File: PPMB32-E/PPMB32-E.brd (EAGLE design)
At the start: 78.7 x 82.2 mm, 11 parts, among them IC1 7805TV, IC2 LM3940IT-3.3, K1 ARK500/2, K2 ARK500/2, K3 ARK500/2, K4 ARK500/2, K5 ARK500/2, U1 ESP32-DEVKITC-32D

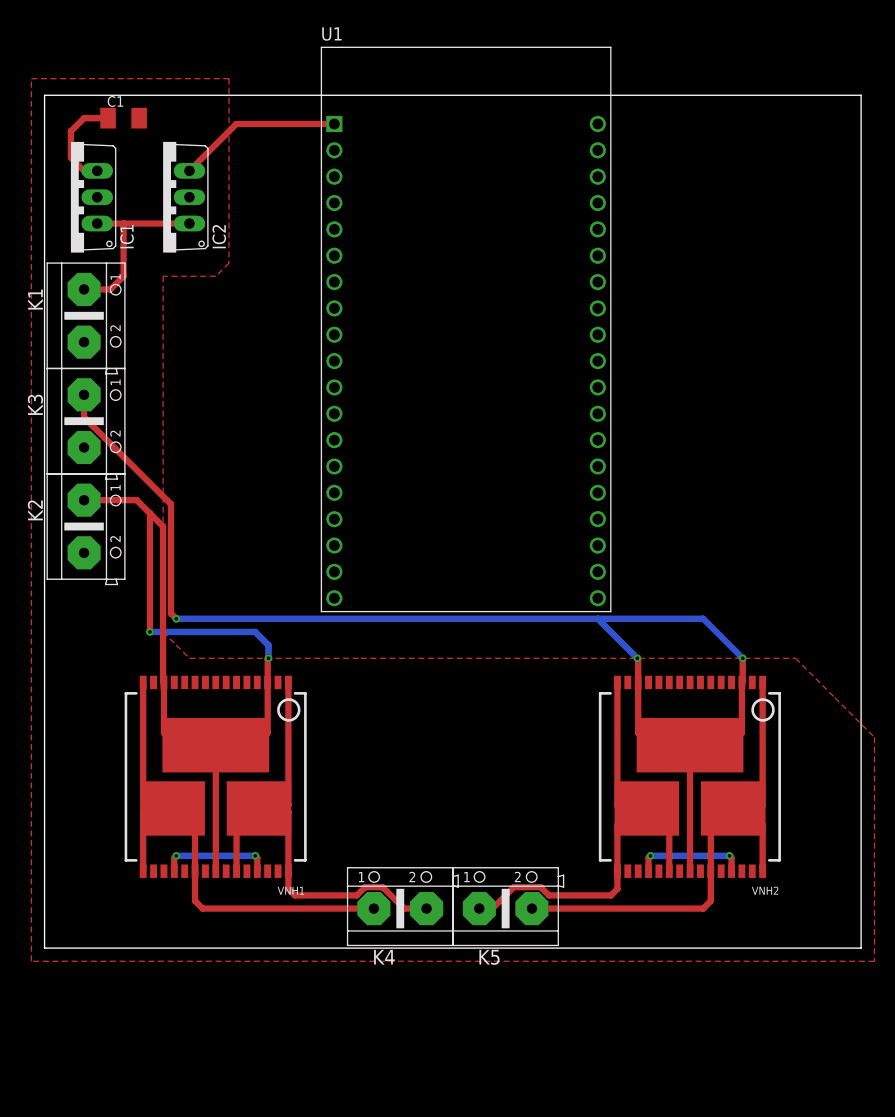
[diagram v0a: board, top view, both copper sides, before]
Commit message: Made progress on PPMB32-E scheme and board. Minor fixes in PPMB32-F board
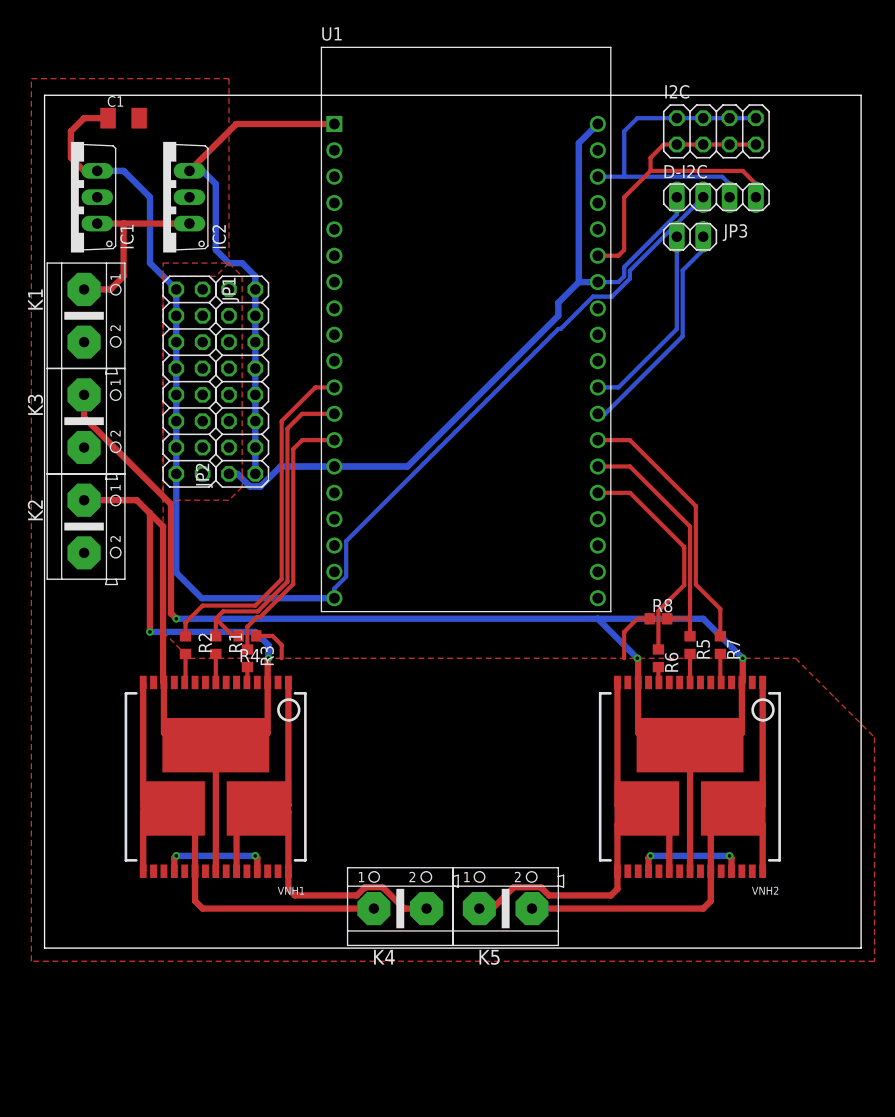
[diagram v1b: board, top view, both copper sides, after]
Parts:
- added D-I2C: (no value), pinhead:1X04
- added I2C: (no value), pinhead:2X04
- added JP1, JP2: (no value), pinhead:2X08
- added JP3: (no value), pinhead:1X02
- added R1, R2, R3, R4, R5, R6, R7, R8: 1k, rcl:R0603
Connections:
- new net I2C_SCL: D-I2C.3, I2C.2, I2C.4, I2C.6, I2C.8, U1.22
- new net I2C_SDA: D-I2C.4, I2C.1, I2C.3, I2C.5, I2C.7, U1.25
- new net N$1: R3.2, VNH1.5
- new net N$2: R2.2, VNH1.11
- new net N$3: R1.2, VNH1.8
- new net N$5: R5.2, VNH2.8
- new net N$6: R6.2, VNH2.11
- new net N$7: R7.2, VNH2.5
- new net UART2_RXD: JP3.2, U1.31
- new net UART2_TXD: JP3.1, U1.30
- net +3V3: now also JP2.1, JP2.11, JP2.13, JP2.15, JP2.3, JP2.5, JP2.7, JP2.9
- net EXT_5V: now also D-I2C.2, JP1.1, JP1.11, JP1.13, JP1.15, JP1.3, JP1.5, JP1.7, JP1.9
- net GND: now also D-I2C.1, JP1.10, JP1.12, JP1.14, JP1.16, JP1.2, JP1.4, JP1.6, JP1.8, JP2.10, JP2.12, JP2.14, JP2.16, JP2.2, JP2.4, JP2.6, JP2.8, R4.1, R8.1
- net VNH1_INA: now also R3.1, U1.13; no longer VNH1.5
- net VNH1_INB: now also R2.1, U1.11; no longer VNH1.11
- net VNH1_PWM: now also R1.1, R4.2, U1.12; no longer VNH1.8
- net VNH2_INA: now also R7.1, U1.32; no longer VNH2.5
- net VNH2_INB: now also R6.1, U1.34; no longer VNH2.11
- net VNH2_PWM: now also R5.1, R8.2, U1.33; no longer VNH2.8
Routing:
- net EXT_5V: track 9.71 -> 123.9 mm
- net GND: track 21.5 -> 104.6 mm
- net I2C_SDA: track 0.00 -> 35.4 mm
- net VNH1_INB: track 0.00 -> 34.0 mm
- net +3V3: track 15.8 -> 49.2 mm
- net VNH1_PWM: track 0.00 -> 32.8 mm
- net I2C_SCL: track 0.00 -> 31.9 mm
- net VNH1_INA: track 0.00 -> 25.6 mm
- net VNH2_INA: track 0.00 -> 25.6 mm
- net VNH2_PWM: track 0.00 -> 24.1 mm
- net UART2_RXD: track 0.00 -> 21.7 mm
- net VNH2_INB: track 0.00 -> 21.4 mm
- net UART2_TXD: track 0.00 -> 18.8 mm
- net N$7: track 0.00 -> 2.78 mm
- net N$2: track 0.00 -> 2.78 mm
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
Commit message: Progress on routing PPMB32-E
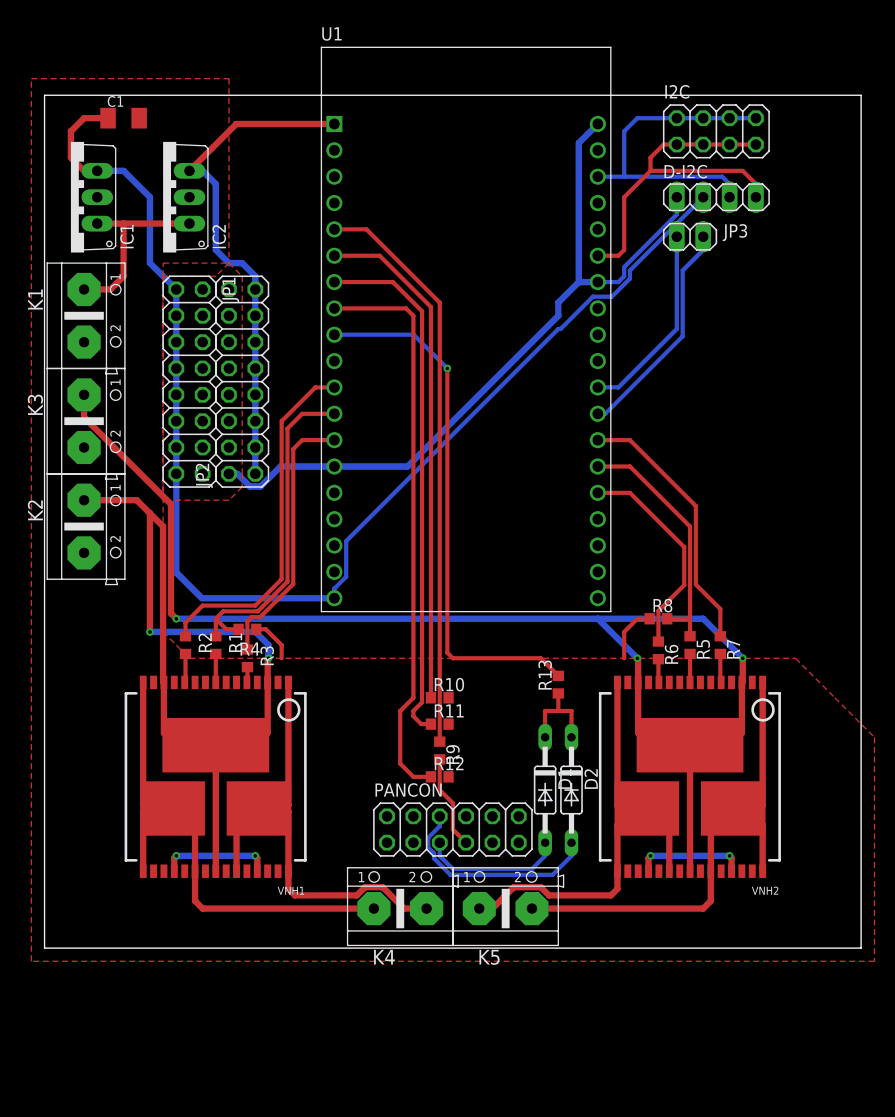
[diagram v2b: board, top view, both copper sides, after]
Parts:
- added D1, D2: 1N4446, diode:DO35-10
- added PANCON: (no value), pinhead:2X06
- added R10, R11, R12, R13, R9: 200R, rcl:R0603
- moved R6 0.76 mm to (59.2, 28.7)
- moved R4 0.64 mm to (19.6, 30.7)
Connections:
- new net N$10: R12.1, U1.8
- new net N$4: R9.1, U1.5
- new net N$8: R10.1, U1.6
- new net N$9: R11.1, U1.7
- new net PANCON_B1: PANCON.7, R9.2
- new net PANCON_B2: PANCON.8, R10.2
- new net PANCON_B3: PANCON.9, R11.2
- new net PANCON_B4: PANCON.10, R12.2
- new net PANCON_M1: PANCON.11
- new net PANCON_M2: PANCON.12
- new net PANCON_W1: D1.A, PANCON.5
- new net PANCON_W2: D2.A, PANCON.6
- new net SVN: U1.4
- new net SVP: U1.3
- new net WOVERRIDE: R13.2, U1.9
- net +3V3: now also PANCON.3
- net EXT_5V: now also PANCON.1
- net GND: now also PANCON.2, PANCON.4
- net VNH1_PWM: now also D1.C, D2.C, R13.1
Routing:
- net N$4: track 0.00 -> 55.4 mm
- net N$10: track 0.00 -> 55.1 mm
- net WOVERRIDE: track 0.00 -> 51.3 mm, vias 0 -> 1
- net N$9: track 0.00 -> 51.0 mm
- net N$8: track 0.00 -> 49.0 mm
- net PANCON_W2: track 0.00 -> 21.3 mm
- net PANCON_W1: track 0.00 -> 13.8 mm
- net PANCON_B1: track 0.00 -> 9.09 mm
- net VNH1_PWM: track 32.8 -> 41.9 mm
- net VNH2_INB: track 21.4 -> 20.6 mm
- net N$6: track 1.50 -> 2.26 mm

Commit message: Major changes in PPMB32-E board and scheme
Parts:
- added C2: 0.33uF, rcl:C1206K
- added C3: 33uF, rcl:C1206K
- added C4: 0.47uF, rcl:C1206K
- added OBDHT: DHT22, diy-modules:TEMP-HUM-SENSOR-DHT22
- moved C1 8.29 mm to (8.38, 71.8), turned to 180 degrees
- moved JP3 6.96 mm to (64.8, 62.1), turned to 180 degrees
- moved IC1 2.84 mm to (1.27, 74.9)
- moved D-I2C 2.54 mm to (62.2, 72.4)
- moved I2C 2.54 mm to (62.2, 78.7)
- moved IC2 1.27 mm to (11.4, 73.7)
- moved R8 0.38 mm to (59.2, 32.1)
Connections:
- new net GPIO23: U1.21
- new net GPIO26: U1.10
- new net GPIO5: U1.29
- new net INTERNAL_SENS: U1.15
- new net N$13: OBDHT.2
- new net ONE_WIRE: U1.35
- new net UART0_RXD: U1.24
- new net UART0_TXD: U1.23
- new net UART2_CTS: U1.27
- new net UART2_RTS: U1.28
- net +3V3: now also C3.1, OBDHT.1
- net EXT_5V: now also C4.1, IC2.1
- net GND: now also C2.2, C3.2, C4.2, OBDHT.4
- net UART2_RXD: now also U1.30; no longer U1.31
- net UART2_TXD: now also U1.31; no longer U1.30
- net VCC: now also C2.1; no longer IC2.1
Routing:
- net +3V3: track 49.2 -> 104.2 mm, vias 0 -> 2
- net VNH1_PWM: track 41.9 -> 84.5 mm, vias 0 -> 2
- net EXT_5V: track 123.9 -> 161.6 mm
- net GND: track 104.8 -> 133.4 mm, vias 4 -> 6
- net UART2_RXD: track 21.7 -> 0.00 mm
- net UART2_TXD: track 18.8 -> 0.00 mm
- net PANCON_B3: track 0.00 -> 15.1 mm
- net PANCON_B2: track 0.00 -> 12.8 mm, vias 0 -> 2
- net PANCON_B4: track 0.00 -> 6.55 mm
- net VCC: track 18.3 -> 12.0 mm
- net I2C_SCL: track 31.9 -> 26.8 mm
- net VNH2_INB: track 20.6 -> 17.8 mm
- net I2C_SDA: track 35.4 -> 33.0 mm
- net VNH2_PWM: track 24.1 -> 22.9 mm
- net VNH2_INA: track 25.6 -> 26.6 mm
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- added copper zone on layer 16, net VNH1_PWR
- added copper zone on layer 16, net VNH2_PWR

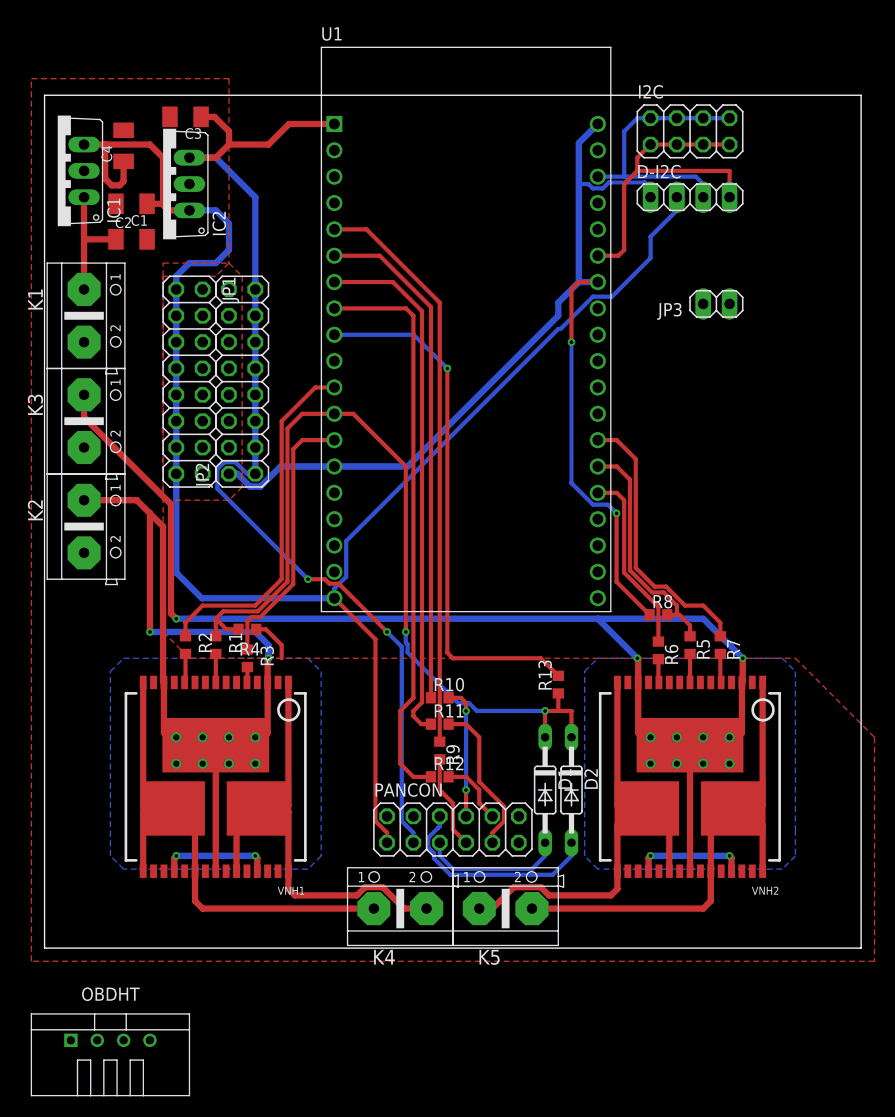
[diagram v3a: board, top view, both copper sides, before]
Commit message: Add pins connected to remaining GPIOs on ESP32devkitC
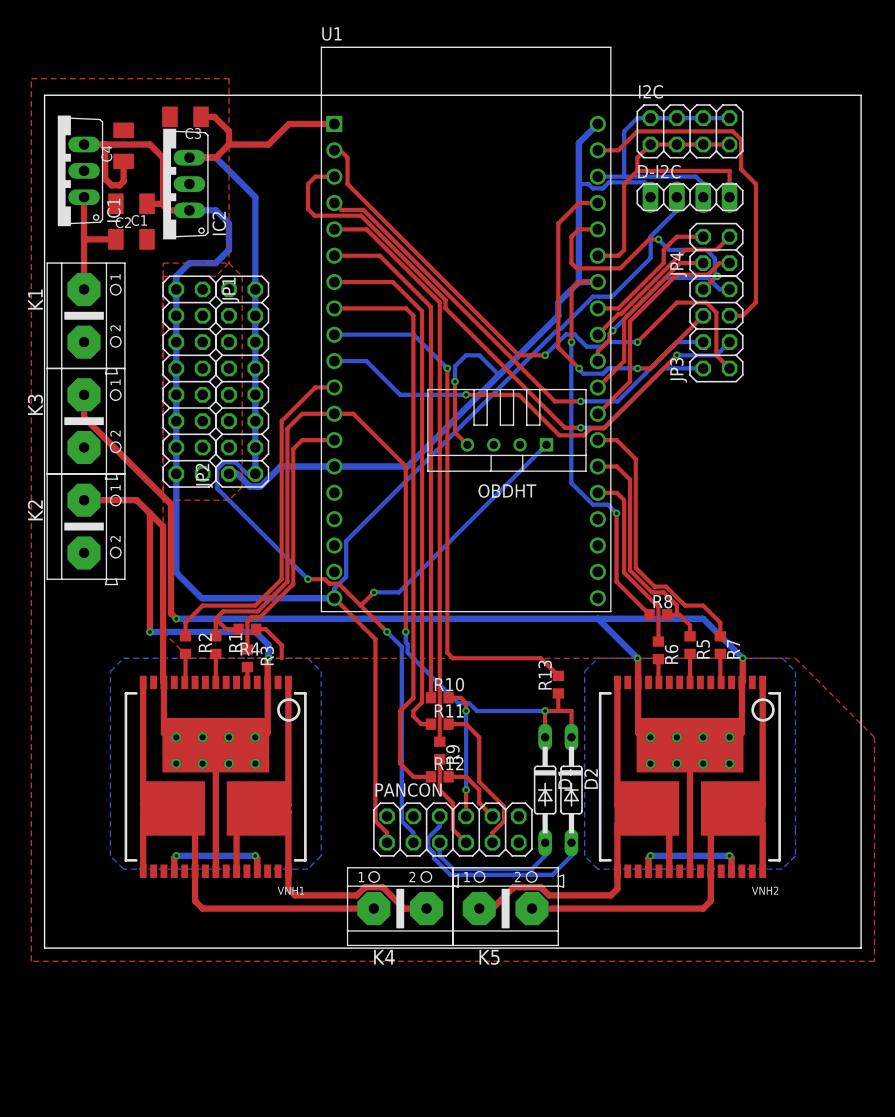
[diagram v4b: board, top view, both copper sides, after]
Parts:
- added JP4: (no value), pinhead:2X02
- JP3: device pinhead:1X02 -> pinhead:2X04
- moved OBDHT 69.0 mm to (44.6, 48.5), turned to 180 degrees
- moved JP3 2.41 mm to (64.8, 59.7), turned to 90 degrees
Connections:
- net ESP_EN: now also JP3.1
- net GPIO23: now also JP3.5
- net GPIO26: now also JP3.3
- net GPIO5: now also JP3.7
- net SVN: now also JP3.4
- net SVP: now also JP3.2
- net UART0_RXD: now also JP3.8
- net UART0_TXD: now also JP3.6
- net UART2_CTS: now also JP4.4
- net UART2_RTS: now also JP4.3
- net UART2_RXD: now also JP4.2; no longer JP3.2
- net UART2_TXD: now also JP4.1; no longer JP3.1
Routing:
- net ESP_EN: track 0.00 -> 55.9 mm, vias 0 -> 2
- net SVP: track 0.00 -> 54.9 mm, vias 0 -> 1
- net SVN: track 0.00 -> 45.8 mm, vias 0 -> 1
- net GPIO26: track 0.00 -> 44.8 mm, vias 0 -> 2
- net GPIO23: track 0.00 -> 34.3 mm
- net UART0_TXD: track 0.00 -> 34.0 mm, vias 0 -> 2
- net UART0_RXD: track 0.00 -> 25.0 mm, vias 0 -> 2
- net +3V3: track 104.2 -> 128.5 mm, vias 2 -> 3
- net UART2_TXD: track 0.00 -> 22.1 mm
- net UART2_RXD: track 0.00 -> 17.5 mm
- net GPIO5: track 0.00 -> 17.4 mm, vias 0 -> 1
- net UART2_RTS: track 0.00 -> 16.6 mm
- net UART2_CTS: track 0.00 -> 13.8 mm
- net GND: track 133.4 -> 146.9 mm, vias 6 -> 7

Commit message: Edit silkscreen on PPMB32-E
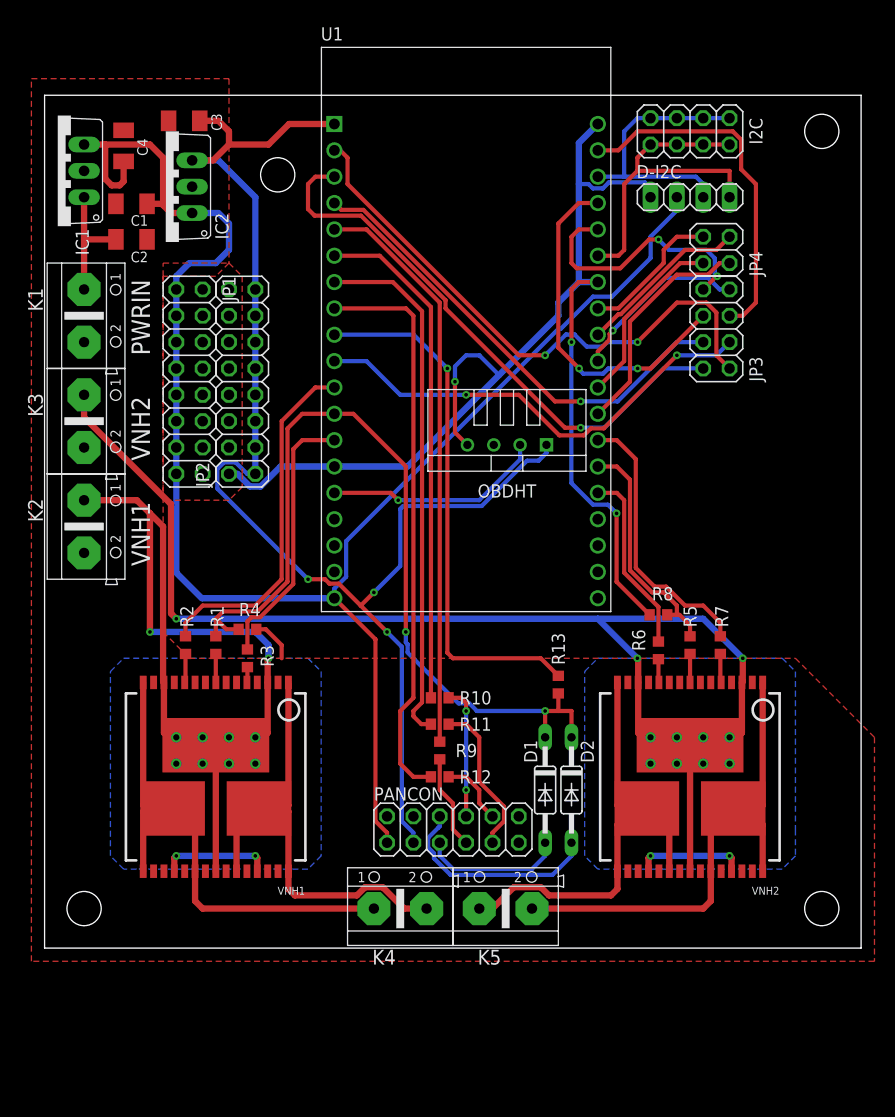
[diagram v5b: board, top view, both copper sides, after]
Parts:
- added U$10, U$7, U$8, U$9: (no value), SparkFun-Hardware:STAND-OFF
- moved C3 0.40 mm to (13.5, 79.8)
- moved IC2 0.36 mm to (11.7, 73.4)
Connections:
- removed net N$13: OBDHT.2
- net INTERNAL_SENS: now also OBDHT.2
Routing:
- net INTERNAL_SENS: track 0.00 -> 21.2 mm, vias 0 -> 1
- net +3V3: track 128.5 -> 131.6 mm
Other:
- board text added: "PWRIN"
- board text added: "VNH1"
- board text added: "VNH2"

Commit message: Edit PPMB32-E; prepare PPSB-T for sending gerbers to JLCPCB
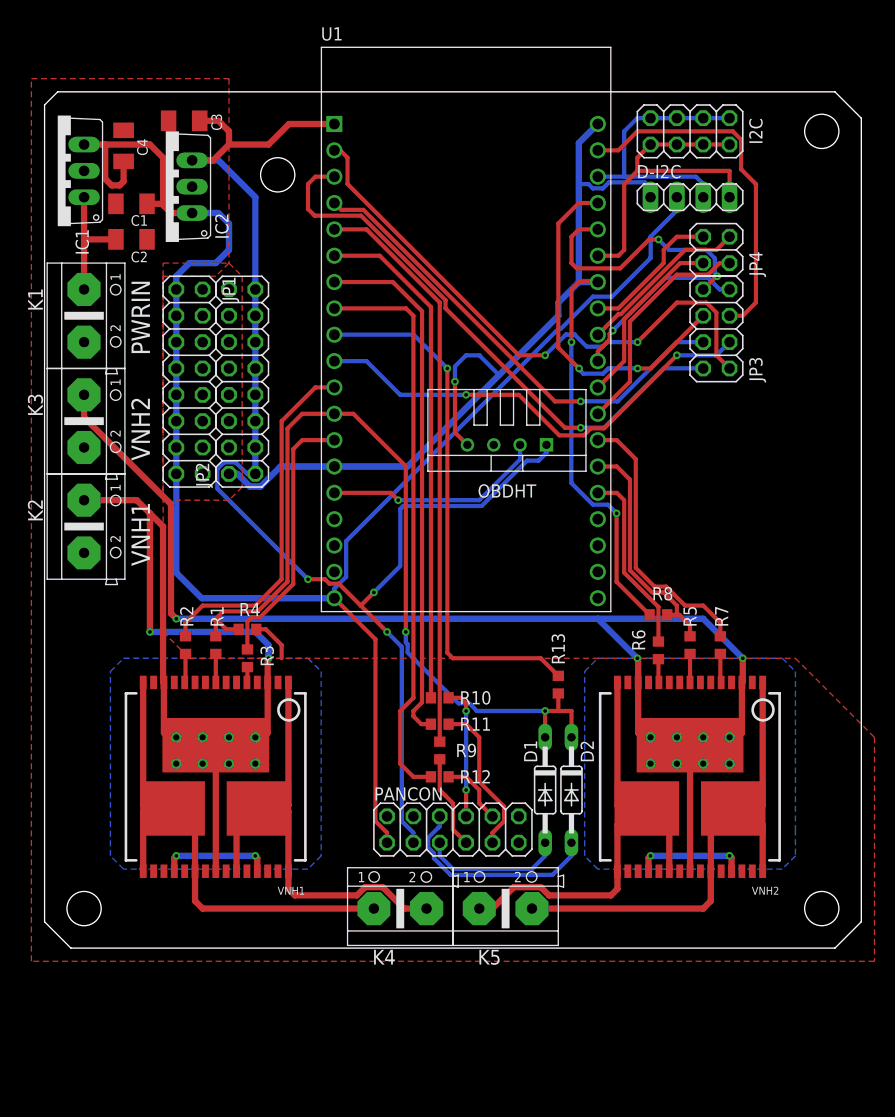
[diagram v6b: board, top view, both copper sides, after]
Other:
- board size 78.7 x 82.2 mm -> 78.7 x 82.5 mm
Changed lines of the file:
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@@
 <drawing>
 <settings>
-<setting alwaysvectorfont="yes"/>
+<setting alwaysvectorfont="no"/>
 <setting verticaltext="up"/>
 </settings>
@@
 </layers>
 <board>
+<fusionsync huburn="a.cGVyc29uYWw6dWUyYzQ3NTBk" projecturn="a.cGVyc29uYWw6dWUyYzQ3NTBkIzIwMjAwMjE0MjY1NTk3Mjc2" f3durn="urn:adsk.wipprod:dm.lineage:Qnsd2eBkTIq1vgTTtXyB2w" pcbguid="dbefda30-5ce9-45df-96e2-1f8c487c71f4" lastpulledtime="" lastsyncedchangeguid="2843f1f9-567a-baaf-3ac9-eb612147a1bb"/>
 <plain>
-<wire x1="0" y1="0" x2="78.72" y2="0" width="0" layer="20"/>
-<wire x1="78.72" y1="0" x2="78.72" y2="82.22" width="0" layer="20"/>
-<wire x1="78.72" y1="82.22" x2="0" y2="82.22" width="0" layer="20"/>
-<wire x1="0" y1="82.22" x2="0" y2="0" width="0" layer="20"/>
 <text x="10.16" y="36.83" size="1.778" layer="25" rot="R90">VNH1</text>
 <text x="10.16" y="46.99" size="1.778" layer="25" rot="R90">VNH2</text>
 <text x="10.16" y="57.15" size="1.778" layer="25" rot="R90">PWRIN</text>
+<wire x1="0" y1="2.54" x2="2.54" y2="0" width="0.0762" layer="20"/>
+<wire x1="2.54" y1="0" x2="76.2" y2="0" width="0.0762" layer="20"/>
+<wire x1="76.2" y1="0" x2="78.74" y2="2.54" width="0.0762" layer="20"/>
+<wire x1="78.74" y1="2.54" x2="78.74" y2="80.01" width="0.0762" layer="20"/>
+<wire x1="78.74" y1="80.01" x2="76.2" y2="82.55" width="0.0762" layer="20"/>
+<wire x1="76.2" y1="82.55" x2="1.27" y2="82.55" width="0.0762" layer="20"/>
+<wire x1="1.27" y1="82.55" x2="0" y2="81.28" width="0.0762" layer="20"/>
+<wire x1="0" y1="81.28" x2="0" y2="2.54" width="0.0762" layer="20"/>
 </plain>
 <attributes>
@@
 </note>
 <note version="8.3" severity="warning">
+Since Version 8.3, EAGLE supports Fusion synchronisation.
+This feature will not be available in this version and saving
+the document will break the link to the Fusion PCB feature.
+</note>
+<note version="8.3" severity="warning">
